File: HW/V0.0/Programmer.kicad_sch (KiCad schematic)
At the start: 37 parts, among them Q11 <name>, Q13 <name>, Q9 <name>, SW2 RESET, U4 PIC32MM

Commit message: PIC16-DevKit-SCH-877 schematic update 1
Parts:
- removed C34, C36: 10uF, symbol Triet_KiCAD_Sym:CAP_CER
- removed H2: PIC32MM-DEBUG, Triet_KiCAD_Fprint:ICSP_Debug, symbol Triet_KiCAD_Sym:ICSP
- removed Q11, Q13, Q9: <name>, symbol Triet_KiCAD_Sym:Mosfet-Nch
- removed R24, R26, R27, R28, R29, R30, R31, R32, R33: 10k, symbol Triet_KiCAD_Sym:RES
- removed TP?: ~{PGM}, Triet_KiCAD_Fprint:TP_SMD, symbol Triet_KiCAD_Sym:TestPoint
- removed TP?: PGD, Triet_KiCAD_Fprint:TP_SMD, symbol Triet_KiCAD_Sym:TestPoint
- removed TP?: PGC, Triet_KiCAD_Fprint:TP_SMD, symbol Triet_KiCAD_Sym:TestPoint
- removed TP?: GND, Triet_KiCAD_Fprint:TP_SMD, symbol Triet_KiCAD_Sym:TestPoint
- removed TP?: ~{MCLR}, Triet_KiCAD_Fprint:TP_SMD, symbol Triet_KiCAD_Sym:TestPoint
- added C25, C26: 100nF, symbol Triet_KiCAD_Sym:CAP_CER
- added D2: 200mA/0.2VF, Liem:SOD-123FL, symbol SAMPI:BAT42
- added L2: IND, symbol SAMPI:IND
- added Q1: MFET N, symbol SAMPI:FET_N-CH
- added Q2: PNP, symbol SAMPI:BJT-PNP
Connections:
- net +5V: now also C25.1, L2.1
- net GND: now also C25.2, C26.2, Q1.2 (S)
- net at C31.1, U4.17 (VCAP): no longer C30.1
- net USB+ renamed USB_P
- net USB- renamed USB_N
- net ~{PG_MCLR_3V3} renamed ~{PG_MCLR}
- new net: D2.A, L2.2, Q1.3 (D)
- new net: C26.1, C30.1, D2.K, Q2.3 (S)
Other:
- moved on the sheet: C31, C32, C33, C35, C37

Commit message: PIC16-DevKit-SCH-877 schematic update 2
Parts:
- removed Q2: PNP, symbol SAMPI:BJT-PNP
- added J1: PG ICSP, symbol SAMPI:SIL06
- added Q2: SI2301DS, symbol SAMPI:FET_P-CH
- added Q5, Q8, Q9: SI2302DS, symbol SAMPI:FET_N-CH
- added R14, R27, R6: 10k, symbol Triet_KiCAD_Sym:RES
- added R15, R24, R28: 2.2k, symbol Triet_KiCAD_Sym:RES
- added R26: 330R, symbol Triet_KiCAD_Sym:RES
- added R5: 100k, symbol Triet_KiCAD_Sym:RES
- C30: value 100nF -> 10uF
- L2: value IND -> 680uH
- Q1: value MFET N -> SI2302DS
- U?: value Level Shifter -> LEVEL SHIFTER
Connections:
- net MOSI_3V3 is gone; now on net TXD: U4.22 (CVREF/AN9/C3INB/RP16/RTCC/U1TX/VBUSON/SDI1/OCM3B/INT1/RB14)
- net TG_PGC/SCLK_3V3 is gone; now on net RXD: U4.23 (AN10/C3INA/REFCLKO/RP17/U1RX/SS1/FSYNC1/OCM2B/INT0/RB15)
- net +3.3V: now also U?.1 (DIR1), J1.2, Q5.1 (G), R14.1, R15.1; no longer D1.1 (A), D3.1 (A), U?.2 (DIR2)
- net +5V: now also R28.1
- net GND: now also R22.2, R23.2, U?.2 (DIR2), J1.3, Q8.2 (S), Q9.2 (S), R24.2; no longer U?.1 (DIR1), U?.8 (DIR4)
- net RXD: no longer U?.12 (B3)
- net TXD: now also U?.3 (A1); no longer U?.11 (B4)
- net ~{PG_MCLR}: now also J1.1
- net at C30.1, D2.K: now also Q2.2 (S), R5.1, R6.1; no longer C26.1
- net VPP_PWM: now reaches Q1.1 (G)
- net SDA: now reaches U4.15 (TMS/REFCLKI/RP14/SDA1/T1CK/T1G/T2CK/T2G/U1RTS/U1BCLK/SDO1/OCM1B/INT2/RB9)
- net PG_LEDPWR renamed PG_PGD
- net PG_PGD: now also J1.4; no longer R22.2
- net PG_LEDSTT renamed PG_PGC
- net PG_PGC: now also J1.5; no longer R23.2
- net TG_PGD/MISO_3V3: no longer names the net of U4.27 (PGEC2/VREF+/CVREF+/AN0/RP1/OCM1E/INT3/RA0)
- net TG_RXD renamed ~{TG_TXD}
- net TG_TXD renamed ~{TG_RXD}
- net U1RX: no longer names the net of U4.7 (OSC2/CLKO/AN6/C3IND/RP4/OCM1D/RA3)
- net U1RX: no longer U?.3 (A1)
- net U1TX: no longer names the net of U4.6 (OSC1/CLKI/AN5/RP3/OCM1C/RA2)
- net U1TX: no longer U?.4 (A2)
- net U2RX: no longer names the net of U4.3 (AN4/C1INB/RP8/SDA2/OCM2E/RB2)
- net U2RX: no longer U?.6 (A4)
- net U2TX: no longer names the net of U4.4 (TDI/AN11/C1INA/RP9/SCL2/OCM2F/RB3)
- net U2TX: no longer U?.5 (A3)
- net VBUS_STT renamed USB_VBUS
- net VDDTG-FB: no longer names the net of U4.28 (PGED2/VREF-/AN1/RP2/OCM1F/RA1)
- net ~{PG_BT}: no longer names the net of U4.16 (PGEC3/TDO/RP18/ASCL1/T3CK/T3G/USBOEN/SDO3/OCM2A/RC9)
- net ~{PG_BT}: no longer SW2.B
- net ~{TG_MCLR_3V3}: no longer names the net of U4.13 (RP12/SDA3/SDI3/OCM3F/RB7)
- net ~{TG_PGM}/~{SRAM_CS_3V3} renamed SCL
- net ~{UART_SEL_3V3}: no longer names the net of U4.11 (PGED3/RP11/ASDA1/USBID/SS3/FSYNC3/OCM3E/RB5)
- net ~{VDDTG_EN}: no longer names the net of U4.21 (AN8/LVDIN/RP15/SCL3/SCK3/OCM3A/RB13)
- new net: Q5.2 (S), R15.2
- new net: Q9.3 (D), R26.2
- new net: Q2.1 (G), R27.1, R5.2
- new net: Q5.3 (D), R28.2
- new net: Q8.3 (D), R27.2
- new net LED_BUSY: D3.1 (A)
- new net LED_STATUS: D1.1 (A)
- new net MCLR: Q9.1 (G)
- new net PGC: U?.5 (A3)
- new net PGD: U?.6 (A4)
- new net PGD_DIR: U?.8 (DIR4)
- new net UTX: U?.4 (A2)
- new net VPP_DIV: R24.1, R6.2
- new net VPP_EN: Q8.1 (G)
- new net ~{BT_MODE}: C26.1, R14.2, SW2.B
- new net ~{TG_MCLR}: Q2.3 (D), R26.1
- new net ~{TG_PGC}: U?.12 (B3)
- new net ~{TG_PGD}: U?.11 (B4)
- no-connect marks 3 -> 1
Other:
- moved on the sheet: C25, C29, C?, D2, L2, Q1, R21, SW2, U?

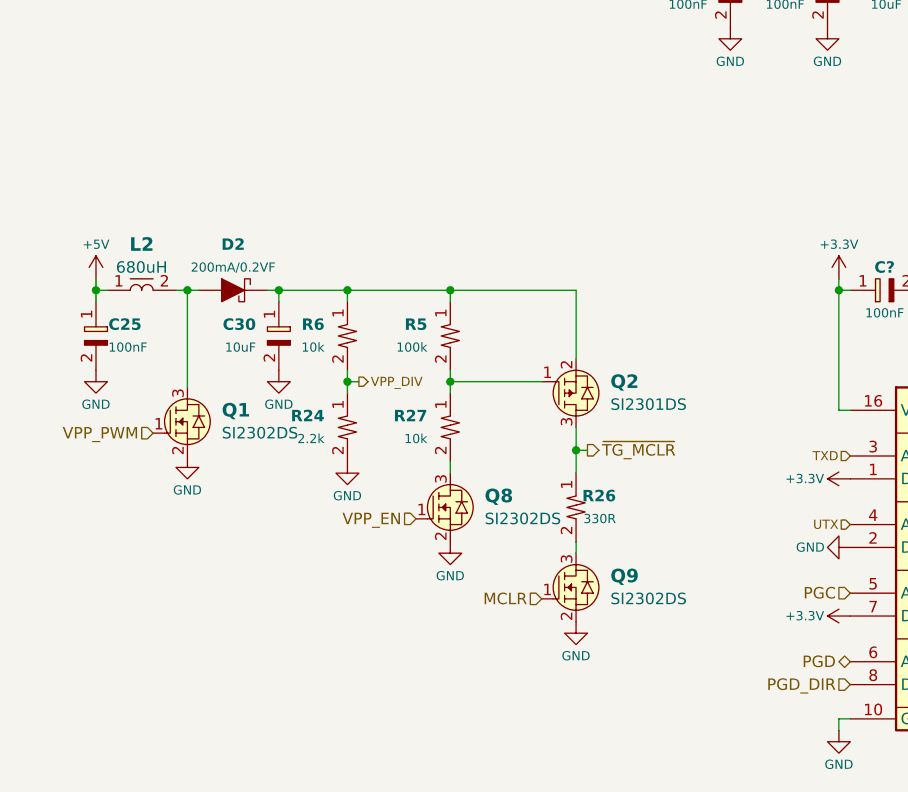
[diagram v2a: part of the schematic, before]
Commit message: PIC16-DevKit-SCH-877 schematic update 3
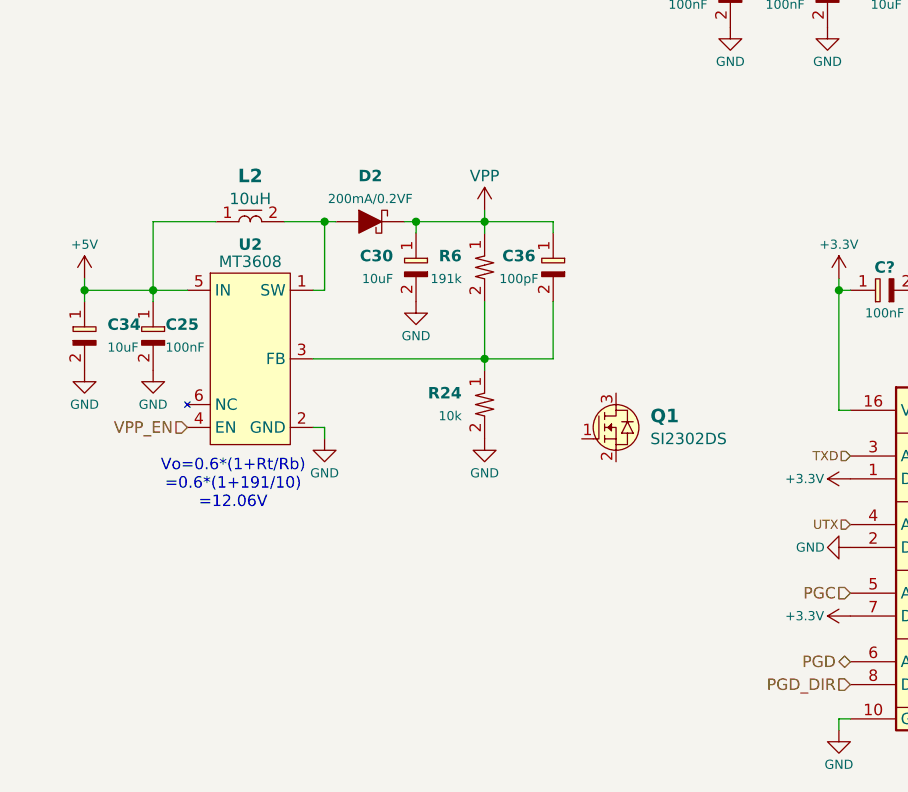
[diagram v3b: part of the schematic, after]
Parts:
- removed Q2: SI2301DS, symbol SAMPI:FET_P-CH
- removed Q8, Q9: SI2302DS, symbol SAMPI:FET_N-CH
- removed R26: 330R, symbol Triet_KiCAD_Sym:RES
- removed R27: 10k, symbol Triet_KiCAD_Sym:RES
- removed R5: 100k, symbol Triet_KiCAD_Sym:RES
- added C34: 10uF, symbol Triet_KiCAD_Sym:CAP_CER
- added C36: 100pF, symbol Triet_KiCAD_Sym:CAP_CER
- added U2: MT3608, symbol SAMPI:MT3608
- L2: value 680uH -> 10uH
- R24: value 2.2k -> 10k
- R6: value 10k -> 191k
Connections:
- net +5V: now also C34.1, U2.5 (IN)
- net GND: now also C34.2, U2.2 (GND); no longer Q1.2 (S)
- net VPP_DIV: no longer R24.1, R6.2
- net VPP_EN: now also U2.4 (EN)
- net VPP_PWM: no longer Q1.1 (G)
- net VPP: now reaches C30.1, D2.K, R6.1
- net VPP: now also C36.1
- net at D2.A, L2.2: now also U2.1 (SW); no longer Q1.3 (D)
- new net: C36.2, R24.1, R6.2, U2.3 (FB)
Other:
- note added: "Vo=0.6*(1+Rt/Rb) =0.6*(1+191/10) =12.06V"
- moved on the sheet: C25, C30, D2, L2, R24, R6

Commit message: PIC16-DevKit-SCH-877 schematic update 4
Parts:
- removed C25: 100nF, symbol Triet_KiCAD_Sym:CAP_CER
- removed C30, C34: 10uF, symbol Triet_KiCAD_Sym:CAP_CER
- removed C36: 100pF, symbol Triet_KiCAD_Sym:CAP_CER
- removed D2: 200mA/0.2VF, Liem:SOD-123FL, symbol SAMPI:BAT42
- removed L2: 10uH, symbol SAMPI:IND
- removed Q5: SI2302DS, symbol SAMPI:FET_N-CH
- removed R15, R28: 2.2k, symbol Triet_KiCAD_Sym:RES
- removed R24: 10k, symbol Triet_KiCAD_Sym:RES
- removed R6: 191k, symbol Triet_KiCAD_Sym:RES
- removed U2: MT3608, symbol SAMPI:MT3608
- added R5: 330R, symbol Triet_KiCAD_Sym:RES
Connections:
- net GND: now also Q1.2 (S)
- net VPP: now also R5.1
- net TG_MCLR: now reaches Q1.1 (G)
- net ~{TG_MCLR}: now reaches Q1.3 (D)
- net ~{TG_MCLR}: now also R5.2
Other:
- note removed: "Vo=0.6*(1+Rt/Rb) =0.6*(1+191/10) =12.06V"
- moved on the sheet: Q1

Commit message: PIC16-DevKit-SCH-877 schematic update 5
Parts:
- removed C? (x2): 100nF, symbol Triet_KiCAD_Sym:CAP_CER
- removed U?: LEVEL SHIFTER, symbol Triet_KiCAD_Sym:ShiftLevel_4CH
- added C23, C24, C30, C31, C33, C34, C35, C36, C37: 100nF, SAMPI:CAP0603, symbol Triet_KiCAD_Sym:CAP_CER
- added Q6, Q7: SI2302DS, SAMPI:SOT23, symbol SAMPI:FET_N-CH
- added R27, R28, R30, R31: 5.1K, 1%, SAMPI:RES0603, symbol Triet_KiCAD_Sym:RES
- added U6, U7, U8, U9: SN74LVC1T45, SAMPI:SOT-23-6_MCHP, symbol SAMPI:LEVEL_SHIFT_1CH
- C22: renamed from C26; footprint (none) -> SAMPI:CAP0603
- C25: renamed from C37; footprint (none) -> SAMPI:CAP0603
- C26: renamed from C35; footprint (none) -> SAMPI:CAP0603
- C27: renamed from C32; footprint (none) -> SAMPI:CAP0603
- C28: renamed from C33; footprint (none) -> SAMPI:CAP0603
- C29: renamed from C31; footprint (none) -> SAMPI:CAP0603
- C32: renamed from C29; footprint (none) -> SAMPI:CAP0603
- D6: renamed from D1; value PWR -> TARGET; footprint (none) -> SAMPI:LED0603
- D7: renamed from D3; value STT -> BUSY; footprint (none) -> SAMPI:LED0603
- J4: renamed from J1; footprint (none) -> SAMPI:HD-1x6x1.27MM-TH
- Q5: renamed from Q1; footprint (none) -> SAMPI:SOT23
- R23: renamed from R14; value 10k -> 10K; footprint (none) -> SAMPI:RES0603
- R24: renamed from R22; footprint (none) -> SAMPI:RES0603
- R25: renamed from R23; footprint (none) -> SAMPI:RES0603
- R26: renamed from R21; value 10k -> 10K; footprint (none) -> SAMPI:RES0603
- R29: renamed from R5; footprint (none) -> SAMPI:RES0603
- SW2: MPN SW603625R2 -> (none)
- renumbered U4 to U5
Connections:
- net +3.3V: now also C24.2, C31.2, C34.2, C36.2, Q6.1 (G), Q7.1 (G), R30.1, R31.1, U6.1 (VCCA), U6.5 (DIR), U7.1 (VCCA), U8.1 (VCCA), U8.5 (DIR), U9.1 (VCCA)
- net GND: now also C23.1, C24.1, C30.1, C31.1, C33.1, C34.1, C35.1, C36.1, C37.2, R28.2, U6.2 (GND), U7.2 (GND), U7.5 (DIR), U8.2 (GND), U9.2 (GND)
- net LED_BUSY: now also D7.A; no longer D7.1 (A)
- net SCL: now also Q6.2 (S), R30.2
- net SDA: now also Q7.2 (S), R31.2
- net TXD: now also U6.3 (A)
- net ~{TG_MCLR}: now also C37.1
- net ~{TG_PGC}: now also U8.4 (B)
- net ~{TG_PGD}: now also R27.2, U9.4 (B)
- net ~{TG_RXD}: now also U6.4 (B)
- net ~{TG_TXD}: now also U7.4 (B)
- net at R25.1: now also D7.K; no longer D7.2 (K)
- net at R24.1: now also D6.K; no longer D6.2 (K)
- removed net LED_STATUS: D6.1 (A)
- net TG_MCLR renamed CS
- new net +VDDTG: C23.2, C30.2, C33.2, C35.2, R27.1, U6.6 (VCCB), U7.6 (VCCB), U8.6 (VCCB), U9.6 (VCCB)
- new net LED_TGRDY: D6.A
- new net SCK: U8.3 (A)
- new net SDI: R28.1, U9.3 (A)
- new net SDO: U9.5 (DIR)
- new net TG_SCL: Q6.3 (D)
- new net TG_SDA: Q7.3 (D)
- new net URX: U7.3 (A)
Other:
- note added: "SPI Write: data should be inverted first SDO=0, B4 is input, B4 pull up, TG_PGD=1. SDO=1, B4 is output, A4 pull down, TG_PGD=0. SPI_XFER(~data); SPI Read: SDO is always low data=SPI_XFER(0x00);"
- moved on the sheet: Q5, R29

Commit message: PIC16-DevKit-SCH-877 schematic update 6
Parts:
- removed SW2: RESET, Triet_KiCAD_Fprint:SW_2P_3.5x6, symbol Triet_KiCAD_Sym:Switch_2P
- removed U5: PIC32MM, Triet_KiCAD_Fprint:UQFN28-EP, symbol Triet_KiCAD_Sym:PIC32MM0064GPM028
- added BT1: MODE, Liem:SW6x6-G, symbol SAMPI:BT2
- added U11: PIC32MM0064GPM028, SAMPI:UQFN28-4x4-EP, symbol SAMPI:PIC32MM0256GPM028-I_M6
- C22, C23, C24, C25, C26, C28, C30, C31, C32, C33, C34, C35, C36, C37: MFT (none) -> Samsung; MNP (none) -> CL10B104KB8NNNC
- C27, C29: MFT (none) -> Samsung; MNP (none) -> CL10A106MQ8NNNC
- D6: MFT (none) -> Harvatek; MNP (none) -> B19Y1NB--20C000113U1930
- D7: MFT (none) -> Harvatek; MNP (none) -> B1911USD-20D000114U1930
- J4: MFT (none) -> DNM; MNP (none) -> NULL; now left out of the parts list
- Q5, Q6, Q7: value SI2302DS -> SI2302; MFT (none) -> Micro Commercial; MNP (none) -> SI2302A-TP
- R23, R26: MFT (none) -> Yageo; MNP (none) -> RC0603JR-0710KL
- R24, R25, R29: MFT (none) -> Yageo; MNP (none) -> RC0603JR-07330RL
- R27, R28, R30, R31: MFT (none) -> Yageo; MNP (none) -> RC0603FR-075K1L
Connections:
- net +3.3V: now also U11.10 (VDD), U11.20 (VUSB3V3), U11.25 (AVDD/VDD)
- net GND: now also BT1.3, BT1.4, U11.24 (AVSS/VSS), U11.29 (EP), U11.5 (VSS)
- net PG_PGC: now also U11.2 (PGEC1/AN3/C1INC/C2INA/RP7/OCM2D/RB1)
- net PG_PGD: now also U11.1 (PGED1/AN2/C1IND/C2INB/C3INC/RP6/OCM2C/RB0)
- net RXD: now also U11.23 (AN10/C3INA/REFCLKO/RP17/U1RX/SS1/FSYNC1/OCM2B/INT0/RB15)
- net SCL: now also U11.14 (TCK/RP13/SCL1/U1CTS/SCK1/OCM1A/RB8)
- net SDA: now also U11.15 (TMS/REFCLKI/RP14/SDA1/T1CK/T1G/T2CK/T2G/U1RTS/U1BCLK/SDO1/OCM1B/INT2/RB9)
- net TXD: now also U11.22 (CVREF/AN9/C3INB/RP16/RTCC/U1TX/VBUSON/SDI1/OCM3B/INT1/RB14)
- net USB_N: now also U11.18 (D-/RB10)
- net USB_P: now also U11.19 (D+/RB11)
- net USB_VBUS: now also U11.12 (VBUS/RB6)
- net ~{BT_MODE}: now also BT1.1, BT1.2
- net ~{PG_MCLR}: now also U11.26 (~{MCLR})
- net at C29.1: now also U11.17 (VCAP)
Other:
- moved on the sheet: C22, C25, C26, C27, C28, C29, C32, J4, R23, R26

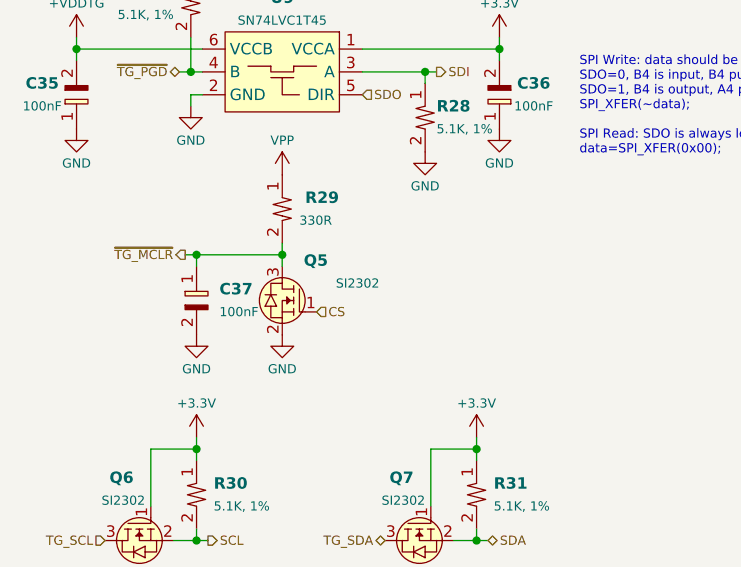
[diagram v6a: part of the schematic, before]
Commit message: PIC16-DevKit-SCH-877 schematic update 7
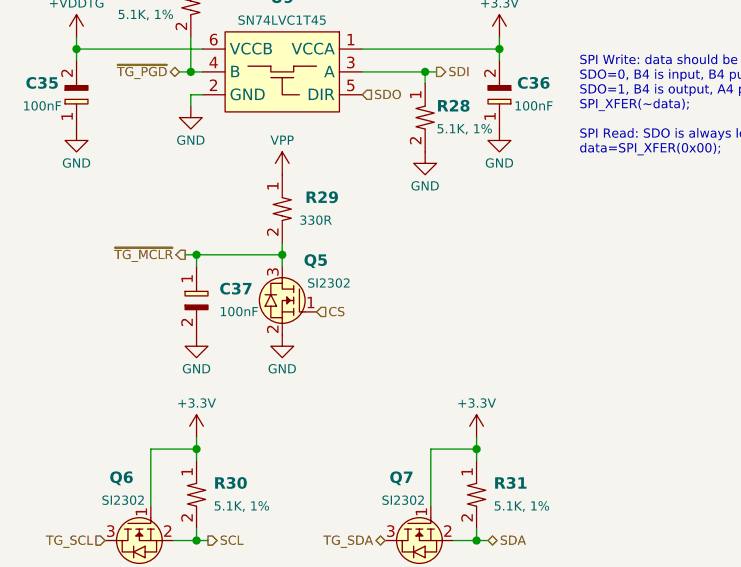
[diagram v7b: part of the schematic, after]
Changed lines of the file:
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@@
 		)
 		(stroke
-			(width 0)
+			(width 0.254)
 			(type default)
 		)
@@
 		)
 		(stroke
-			(width 0)
+			(width 0.254)
 			(type default)
 		)
@@
 		)
 		(stroke
-			(width 0)
+			(width 0.254)
 			(type default)
 		)
@@
 		)
 		(stroke
-			(width 0)
+			(width 0.254)
 			(type default)
 		)
@@
 		)
 		(stroke
-			(width 0)
+			(width 0.254)
 			(type default)
 		)
@@
 		)
 		(stroke
-			(width 0)
+			(width 0.254)
 			(type default)
 		)
@@
 		)
 		(stroke
-			(width 0)
+			(width 0.254)
 			(type default)
 		)
@@
 		)
 		(stroke
-			(width 0)
+			(width 0.254)
 			(type default)
 		)
@@
 		)
 		(stroke
-			(width 0)
+			(width 0.254)
 			(type default)
 		)
@@
 		)
 		(stroke
-			(width 0)
+			(width 0.254)
 			(type default)
 		)
@@
 		)
 		(stroke
-			(width 0)
+			(width 0.254)
 			(type default)
 		)
@@
 		)
 		(stroke
-			(width 0)
+			(width 0.254)
 			(type default)
 		)
@@
 		)
 		(stroke
-			(width 0)
+			(width 0.254)
 			(type default)
 		)
@@
 		)
 		(stroke
-			(width 0)
+			(width 0.254)
 			(type default)
 		)
@@
 		)
 		(stroke
-			(width 0)
+			(width 0.254)
 			(type default)
 		)
@@
 		)
 		(stroke
-			(width 0)
+			(width 0.254)
 			(type default)
 		)
@@
 		)
 		(stroke
-			(width 0)
+			(width 0.254)
 			(type default)
 		)
@@
 		)
 		(stroke
-			(width 0)
+			(width 0.254)
 			(type default)
 		)
@@
 		)
 		(stroke
-			(width 0)
+			(width 0.254)
 			(type default)
 		)
@@
 		)
 		(stroke
-			(width 0)
+			(width 0.254)
 			(type default)
 		)
@@
 		)
 		(stroke
-			(width 0)
+			(width 0.254)
 			(type default)
 		)
@@
 		)
 		(stroke
-			(width 0)
+			(width 0.254)
 			(type default)
 		)
@@
 		)
 		(stroke
-			(width 0)
+			(width 0.254)
 			(type default)
 		)
@@
 		)
 		(stroke
-			(width 0)
+			(width 0.254)
 			(type default)
 		)
@@
 		)
 		(stroke
-			(width 0)
+			(width 0.254)
 			(type default)
 		)
@@
 		)
 		(stroke
-			(width 0)
+			(width 0.254)
 			(type default)
 		)
@@
 		)
 		(stroke
-			(width 0)
+			(width 0.254)
 			(type default)
 		)
@@
 		)
 		(stroke
-			(width 0)
+			(width 0.254)
 			(type default)
 		)
@@
 		)
 		(stroke
-			(width 0)
+			(width 0.254)
 			(type default)
 		)
@@
 		)
 		(stroke
-			(width 0)
+			(width 0.254)
 			(type default)
 		)
@@
 		)
 		(stroke
-			(width 0)
+			(width 0.254)
 			(type default)
 		)
@@
 		)
 		(stroke
-			(width 0)
+			(width 0.254)
 			(type default)
 		)
@@
 		)
 		(stroke
-			(width 0)
+			(width 0.254)
 			(type default)
 		)
@@
 		)
 		(stroke
-			(width 0)
+			(width 0.254)
 			(type default)
 		)
@@
 		)
 		(stroke
-			(width 0)
+			(width 0.254)
 			(type default)
 		)
@@
 		)
 		(stroke
-			(width 0)
+			(width 0.254)
 			(type default)
 		)
@@
 		)
 		(stroke
-			(width 0)
+			(width 0.254)
 			(type default)
 		)
@@
 		)
 		(stroke
-			(width 0)
+			(width 0.254)
 			(type default)
 		)
@@
 		)
 		(stroke
-			(width 0)
+			(width 0.254)
 			(type default)
 		)
@@
 		)
 		(stroke
-			(width 0)
+			(width 0.254)
 			(type default)
 		)
@@
 		)
 		(stroke
-			(width 0)
+			(width 0.254)
 			(type default)
 		)
@@
 		)
 		(stroke
-			(width 0)
+			(width 0.254)
 			(type default)
 		)
@@
 		)
 		(property "Value" "SI2302"
-			(at 52.705 154.305 0)
+			(at 49.53 154.305 0)
 			(effects
 				(font

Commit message: PIC16-DevKit-PCB-877 layout update 1
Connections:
- net LED_BUSY: now also U11.9 (SOSCO/SCLKI/RP5/PWRLCLK/OCM3D/RA4)
- net LED_TGRDY: now also U11.8 (SOSCI/AN7/RP10/OCM3C/RB4)
- net VPP_EN: now also U11.6 (OSC1/CLKI/AN5/RP3/OCM1C/RA2)
- net ~{VTG_EN}: now also U11.7 (OSC2/CLKO/AN6/C3IND/RP4/OCM1D/RA3)
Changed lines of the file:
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@@
 	(hierarchical_label "SDO"
 		(shape input)
-		(at 232.41 34.29 0)
+		(at 244.475 20.955 0)
 		(fields_autoplaced yes)
 		(effects
@@
 	(hierarchical_label "VPP_EN"
 		(shape output)
-		(at 232.41 41.91 0)
+		(at 142.24 29.21 180)
 		(fields_autoplaced yes)
 		(effects
@@
 				(thickness 0.254)
 			)
-			(justify left)
+			(justify right)
 		)
 	)
@@
 	(hierarchical_label "SDI"
 		(shape output)
-		(at 232.41 31.75 0)
+		(at 244.475 18.415 0)
 		(fields_autoplaced yes)
 		(effects
@@
 	(hierarchical_label "LED_BUSY"
 		(shape output)
-		(at 139.7 26.67 180)
+		(at 142.24 34.29 180)
 		(fields_autoplaced yes)
 		(effects
@@
 	(hierarchical_label "CS"
 		(shape output)
-		(at 232.41 36.83 0)
+		(at 242.57 23.495 0)
 		(fields_autoplaced yes)
 		(effects
@@
 	(hierarchical_label "LED_TGRDY"
 		(shape output)
-		(at 139.7 29.21 180)
+		(at 231.14 34.29 0)
 		(fields_autoplaced yes)
 		(effects
@@
 				(size 1.016 1.016)
 			)
-			(justify right)
+			(justify left)
 		)
 	)
@@
 	(hierarchical_label "SCK"
 		(shape input)
-		(at 232.41 29.21 0)
+		(at 242.57 15.875 0)
 		(fields_autoplaced yes)
 		(effects
@@
 	(hierarchical_label "~{VTG_EN}"
 		(shape output)
-		(at 232.41 54.61 0)
+		(at 142.24 31.75 180)
 		(fields_autoplaced yes)
 		(effects
@@
 				(thickness 0.254)
 			)
-			(justify left)
+			(justify right)
 		)
 	)
@@
 		(on_board yes)
 		(dnp no)
-		(fields_autoplaced yes)
 		(property "Reference" "C27"
 			(at 121.285 60.9599 0)
@@
 		)
 		(instances
-			(project ""
+			(project "PIC16DevKit"
 				(path "/17281b91-3f9a-4e36-96b2-66002b412b3a/6fab4358-8edb-4c81-8f5e-6901c5551004"
 					(reference "U6")
@@
 		(on_board yes)
 		(dnp no)
-		(fields_autoplaced yes)
 		(property "Reference" "C25"
 			(at 105.41 60.9599 0)
@@
 		)
 		(instances
-			(project ""
+			(project "PIC16DevKit"
 				(path "/17281b91-3f9a-4e36-96b2-66002b412b3a/6fab4358-8edb-4c81-8f5e-6901c5551004"
 					(reference "U11")
@@
 		)
 		(instances
-			(project ""
+			(project "PIC16DevKit"
 				(path "/17281b91-3f9a-4e36-96b2-66002b412b3a/6fab4358-8edb-4c81-8f5e-6901c5551004"
 					(reference "BT1")
